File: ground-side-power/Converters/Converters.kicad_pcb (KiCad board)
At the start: 2 copper layers, 82.8 x 74.4 mm, 36 parts, among them J10 Conn_01x03_Female, J12 Conn_01x04_Female, J13 DAQ Voltage Sensing, J14 DAQ Current Sensing, J27 Conn_01x02_Female, U3 K7805-3AR3, U4 INA180, U5 INA180, U6 URB2424LD-20WR3

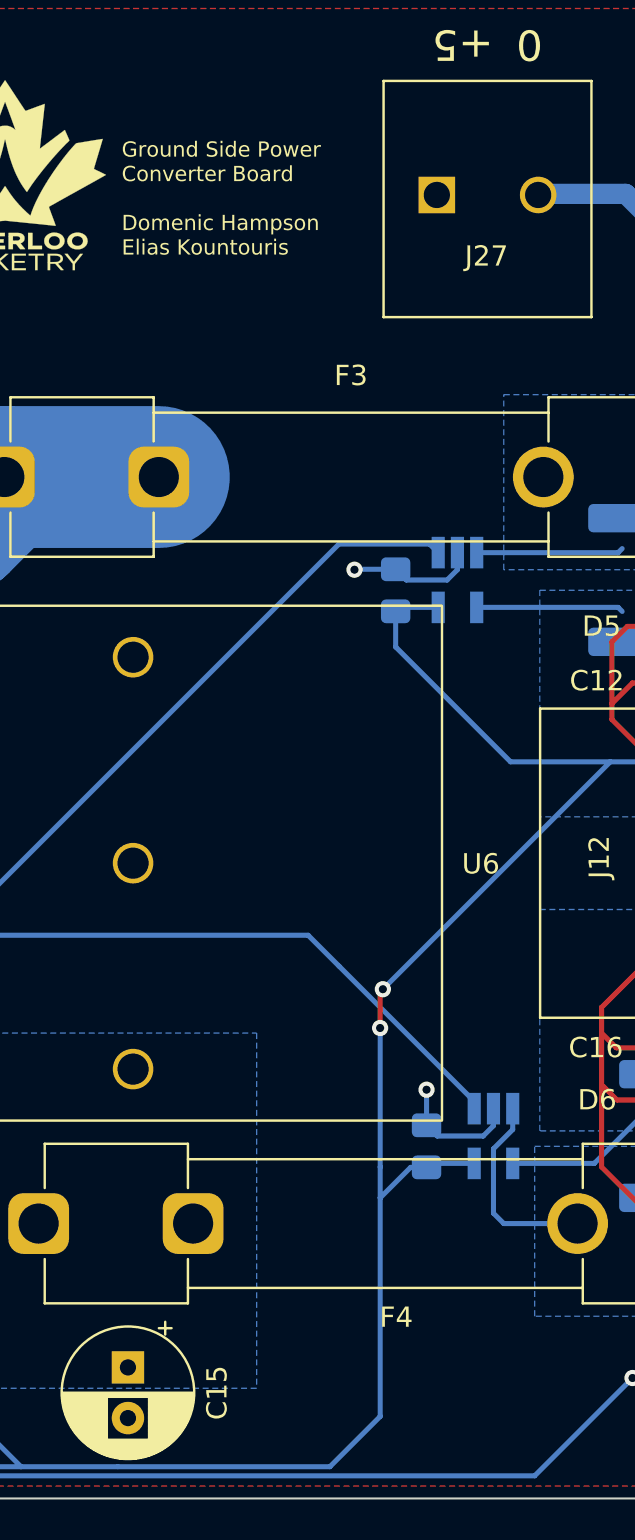
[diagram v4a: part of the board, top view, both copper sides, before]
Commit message: Silkscreen and current sense changes
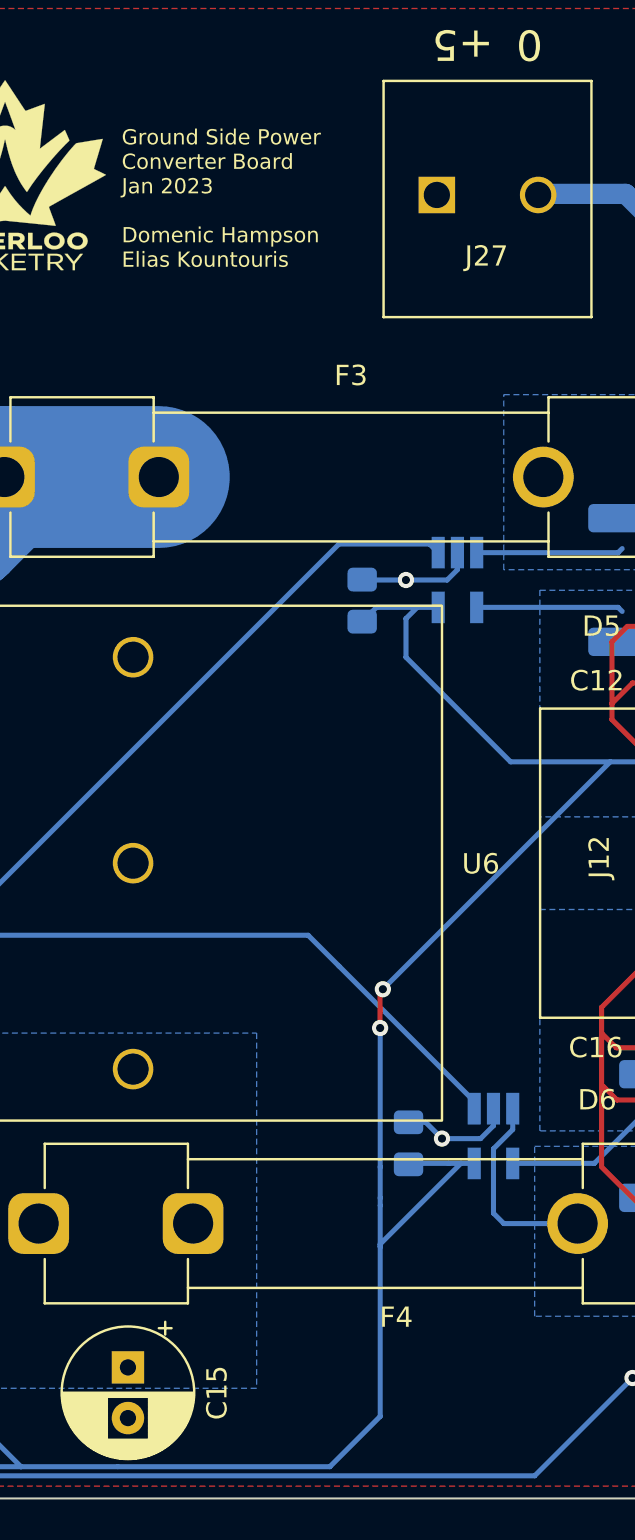
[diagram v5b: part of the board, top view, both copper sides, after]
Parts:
- moved C9 1.73 mm to (161.2, 96.5)
- moved C13 0.90 mm to (163.4, 123.3)
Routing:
- net +5V: track 152.5 -> 158.2 mm
- net GND: track 28.0 -> 26.2 mm
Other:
- board text added: "Ground Side Power Converter Board Jan 2023 Domenic Hampson Elias Kountouris"
- board text removed: "Ground Side Power Converter Board Domenic Hampson Elias Kountouris"
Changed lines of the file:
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@@
   )
   (footprint "Capacitor_SMD:C_0805_2012Metric_Pad1.18x1.45mm_HandSolder" (layer "B.Cu")
-    (at 164.338 123.444 -90)
+    (at 163.449 123.2955 -90)
     (descr "Capacitor SMD 0805 (2012 Metric), square (rectangular) end terminal, IPC_7351 nominal with elongated pad for handsoldering. (Body size source: IPC-SM-782 page 76, https://www.pcb-3d.com/wordpress/wp-content/uploads/ipc-sm-782a_amendment_1_and_2.pdf, https://docs.google.com/spreadsheets/d/1BsfQQcO9C6DZCsRaXUlFlo91Tg2WpOkGARC1WS5S8t0/edit?usp=sharing), generated with kicad-footprint-generator")
     (tags "capacitor handsolder")
@@
   )
   (footprint "Capacitor_SMD:C_0805_2012Metric_Pad1.18x1.45mm_HandSolder" (layer "B.Cu")
-    (at 162.814 96.012 -90)
+    (at 161.163 96.52 -90)
     (descr "Capacitor SMD 0805 (2012 Metric), square (rectangular) end terminal, IPC_7351 nominal with elongated pad for handsoldering. (Body size source: IPC-SM-782 page 76, https://www.pcb-3d.com/wordpress/wp-content/uploads/ipc-sm-782a_amendment_1_and_2.pdf, https://docs.google.com/spreadsheets/d/1BsfQQcO9C6DZCsRaXUlFlo91Tg2WpOkGARC1WS5S8t0/edit?usp=sharing), generated with kicad-footprint-generator")
     (tags "capacitor handsolder")
@@
     (effects (font (size 1.5 1.5) (thickness 0.3)))
   )
-  (gr_text "Ground Side Power\nConverter Board\n\nDomenic Hampson \nElias Kountouris" (at 149.294 76.684) (layer "F.SilkS")
+  (gr_text "Ground Side Power\nConverter Board\nJan 2023\n\nDomenic Hampson \nElias Kountouris" (at 149.294 76.684) (layer "F.SilkS")
     (effects (font (size 0.75 0.75) (thickness 0.15)) (justify left))
   )
@@
     (effects (font (size 1.5 1.5) (thickness 0.3)))
   )
-  (via (at 160.782 94.996) (size 0.8) (drill 0.4) (layers "F.Cu" "B.Cu") (net 1))
+  (via (at 163.322 95.504) (size 0.8) (drill 0.4) (layers "F.Cu" "B.Cu") (net 1))
   (via (at 133.35 135.636) (size 0.8) (drill 0.4) (layers "F.Cu" "B.Cu") (net 1))
-  (via (at 164.338 120.65) (size 0.8) (drill 0.4) (layers "F.Cu" "B.Cu") (net 1))
+  (via (at 165.1 123.063) (size 0.8) (drill 0.4) (layers "F.Cu" "B.Cu") (net 1))
   (via (at 123.19 135.636) (size 0.8) (drill 0.4) (layers "F.Cu" "B.Cu") (net 1))
   (via (at 112.014 138.684) (size 0.8) (drill 0.4) (layers "F.Cu" "B.Cu") (net 1))
-  (segment (start 164.338 122.4065) (end 164.338 120.65) (width 0.25) (layer "B.Cu") (net 1))
   (segment (start 125.1215 91.186) (end 125.1215 88.7465) (width 0.25) (layer "B.Cu") (net 1))
-  (segment (start 163.3435 95.504) (end 165.354 95.504) (width 0.25) (layer "B.Cu") (net 1))
-  (segment (start 162.814 94.9745) (end 160.8035 94.9745) (width 0.25) (layer "B.Cu") (net 1))
+  (segment (start 167.005 123.063) (end 167.64 122.428) (width 0.25) (layer "B.Cu") (net 1))
   (segment (start 114.824 137.16) (end 113.538 137.16) (width 0.25) (layer "B.Cu") (net 1))
-  (segment (start 160.8035 94.9745) (end 160.782 94.996) (width 0.25) (layer "B.Cu") (net 1))
   (segment (start 113.538 137.16) (end 112.014 138.684) (width 0.25) (layer "B.Cu") (net 1))
+  (segment (start 167.64 122.428) (end 167.64 121.586) (width 0.25) (layer "B.Cu") (net 1))
+  (segment (start 165.1 123.063) (end 167.005 123.063) (width 0.25) (layer "B.Cu") (net 1))
   (segment (start 125.289 88.579) (end 125.289 87.63) (width 0.25) (layer "B.Cu") (net 1))
   (segment (start 120.209 90.7115) (end 120.209 87.63) (width 0.25) (layer "B.Cu") (net 1))
-  (segment (start 164.8675 122.936) (end 167.132 122.936) (width 0.25) (layer "B.Cu") (net 1))
   (segment (start 165.354 95.504) (end 165.862 94.996) (width 0.25) (layer "B.Cu") (net 1))
   (segment (start 124.714 137.16) (end 123.19 135.636) (width 0.25) (layer "B.Cu") (net 1))
-  (segment (start 162.814 94.9745) (end 163.3435 95.504) (width 0.25) (layer "B.Cu") (net 1))
-  (segment (start 167.64 122.428) (end 167.64 121.586) (width 0.25) (layer "B.Cu") (net 1))
+  (segment (start 164.295 122.258) (end 165.1 123.063) (width 0.25) (layer "B.Cu") (net 1))
   (segment (start 134.636 137.16) (end 134.636 136.922) (width 0.25) (layer "B.Cu") (net 1))
+  (segment (start 163.449 122.258) (end 164.295 122.258) (width 0.25) (layer "B.Cu") (net 1))
   (segment (start 119.7345 91.186) (end 120.209 90.7115) (width 0.25) (layer "B.Cu") (net 1))
+  (segment (start 163.322 95.504) (end 161.6925 95.504) (width 0.25) (layer "B.Cu") (net 1))
   (segment (start 125.1215 88.7465) (end 125.289 88.579) (width 0.25) (layer "B.Cu") (net 1))
-  (segment (start 164.338 122.4065) (end 164.8675 122.936) (width 0.25) (layer "B.Cu") (net 1))
-  (segment (start 167.132 122.936) (end 167.64 122.428) (width 0.25) (layer "B.Cu") (net 1))
   (segment (start 124.984 137.16) (end 124.714 137.16) (width 0.25) (layer "B.Cu") (net 1))
   (segment (start 165.862 94.996) (end 165.862 94.154) (width 0.25) (layer "B.Cu") (net 1))
   (segment (start 134.636 136.922) (end 133.35 135.636) (width 0.25) (layer "B.Cu") (net 1))
+  (segment (start 165.354 95.504) (end 163.322 95.504) (width 0.25) (layer "B.Cu") (net 1))
   (segment (start 174.498 100.584) (end 173.482 101.6) (width 0.25) (layer "F.Cu") (net 2))
   (segment (start 173.482 98.552) (end 174.244 97.79) (width 0.25) (layer "F.Cu") (net 2))
@@
   (via (at 162.047701 117.606299) (size 0.8) (drill 0.4) (layers "F.Cu" "B.Cu") (net 2))
   (via (at 162.183299 115.692701) (size 0.8) (drill 0.4) (layers "F.Cu" "B.Cu") (net 2))
-  (segment (start 162.814 98.806) (end 168.482001 104.474001) (width 0.25) (layer "B.Cu") (net 2))
+  (segment (start 163.322 97.409) (end 163.322 99.314) (width 0.25) (layer "B.Cu") (net 2))
+  (segment (start 163.877 96.854) (end 161.8665 96.854) (width 0.25) (layer "B.Cu") (net 2))
+  (segment (start 161.8665 96.854) (end 161.163 97.5575) (width 0.25) (layer "B.Cu") (net 2))
   (segment (start 159.57 139.25) (end 162.052 136.768) (width 0.25) (layer "B.Cu") (net 2))
-  (segment (start 163.0095 96.854) (end 162.814 97.0495) (width 0.25) (layer "B.Cu") (net 2))
-  (segment (start 164.5335 124.286) (end 164.338 124.4815) (width 0.25) (layer "B.Cu") (net 2))
-  (segment (start 164.912 96.854) (end 163.0095 96.854) (width 0.25) (layer "B.Cu") (net 2))
+  (segment (start 168.482001 104.474001) (end 173.401999 104.474001) (width 0.25) (layer "B.Cu") (net 2))
   (segment (start 162.052 125.984) (end 162.052 124.46) (width 0.25) (layer "B.Cu") (net 2))
   (segment (start 162.183299 115.692701) (end 173.401999 104.474001) (width 0.25) (layer "B.Cu") (net 2))
@@
   (segment (start 142.52 137.44) (end 144.33 139.25) (width 0.25) (layer "B.Cu") (net 2))
   (segment (start 142.52 137.16) (end 142.52 137.44) (width 0.25) (layer "B.Cu") (net 2))
-  (segment (start 168.482001 104.474001) (end 173.401999 104.474001) (width 0.25) (layer "B.Cu") (net 2))
+  (segment (start 163.322 99.314) (end 168.482001 104.474001) (width 0.25) (layer "B.Cu") (net 2))
   (segment (start 133.662 139.25) (end 144.33 139.25) (width 0.25) (layer "B.Cu") (net 2))
   (segment (start 162.052 124.46) (end 162.052 117.610598) (width 0.25) (layer "B.Cu") (net 2))
-  (segment (start 164.338 124.4815) (end 163.5545 124.4815) (width 0.25) (layer "B.Cu") (net 2))
+  (segment (start 166.69 124.286) (end 166.036 124.286) (width 0.25) (layer "B.Cu") (net 2))
+  (segment (start 165.434 124.286) (end 163.623 124.286) (width 0.25) (layer "B.Cu") (net 2))
   (segment (start 173.79 96.854) (end 166.812 96.854) (width 0.25) (layer "B.Cu") (net 2))
   (segment (start 175.567999 104.474001) (end 181.102 98.94) (width 1) (layer "B.Cu") (net 2))
+  (segment (start 162.052 136.768) (end 162.052 128.397) (width 0.25) (layer "B.Cu") (net 2))
+  (segment (start 164.912 96.854) (end 163.877 96.854) (width 0.25) (layer "B.Cu") (net 2))
   (segment (start 173.99 97.054) (end 173.79 96.854) (width 0.25) (layer "B.Cu") (net 2))
+  (segment (start 162.052 126.365) (end 162.052 125.984) (width 0.25) (layer "B.Cu") (net 2))
   (segment (start 131.572 137.16) (end 133.662 139.25) (width 0.25) (layer "B.Cu") (net 2))
+  (segment (start 162.052 128.397) (end 162.052 126.365) (width 0.25) (layer "B.Cu") (net 2))
   (segment (start 162.052 117.610598) (end 162.047701 117.606299) (width 0.25) (layer "B.Cu") (net 2))
-  (segment (start 162.052 136.768) (end 162.052 125.984) (width 0.25) (layer "B.Cu") (net 2))
-  (segment (start 162.814 97.0495) (end 162.814 98.806) (width 0.25) (layer "B.Cu") (net 2))
-  (segment (start 163.5545 124.4815) (end 162.052 125.984) (width 0.25) (layer "B.Cu") (net 2))
-  (segment (start 166.69 124.286) (end 164.5335 124.286) (width 0.25) (layer "B.Cu") (net 2))
+  (segment (start 166.036 124.286) (end 165.434 124.286) (width 0.25) (layer "B.Cu") (net 2))
+  (segment (start 163.877 96.854) (end 163.322 97.409) (width 0.25) (layer "B.Cu") (net 2))
   (segment (start 173.401999 104.474001) (end 175.567999 104.474001) (width 0.25) (layer "B.Cu") (net 2))
   (segment (start 149.098 139.25) (end 159.57 139.25) (width 0.25) (layer "B.Cu") (net 2))
+  (segment (start 162.052 128.27) (end 162.052 128.397) (width 0.25) (layer "B.Cu") (net 2))
+  (segment (start 166.036 124.286) (end 162.052 128.27) (width 0.25) (layer "B.Cu") (net 2))
   (segment (start 181.102 98.94) (end 181.102 83.392) (width 1) (layer "B.Cu") (net 2))
   (segment (start 181.102 83.392) (end 174.164 76.454) (width 1) (layer "B.Cu") (net 2))
+  (segment (start 163.623 124.286) (end 163.576 124.333) (width 0.25) (layer "B.Cu") (net 2))
   (segment (start 132.468 91.186) (end 132.909 90.745) (width 0.25) (layer "B.Cu") (net 3))
   (segment (start 143.51 90.424) (end 151.13 90.424) (width 7) (layer "B.Cu") (net 3))

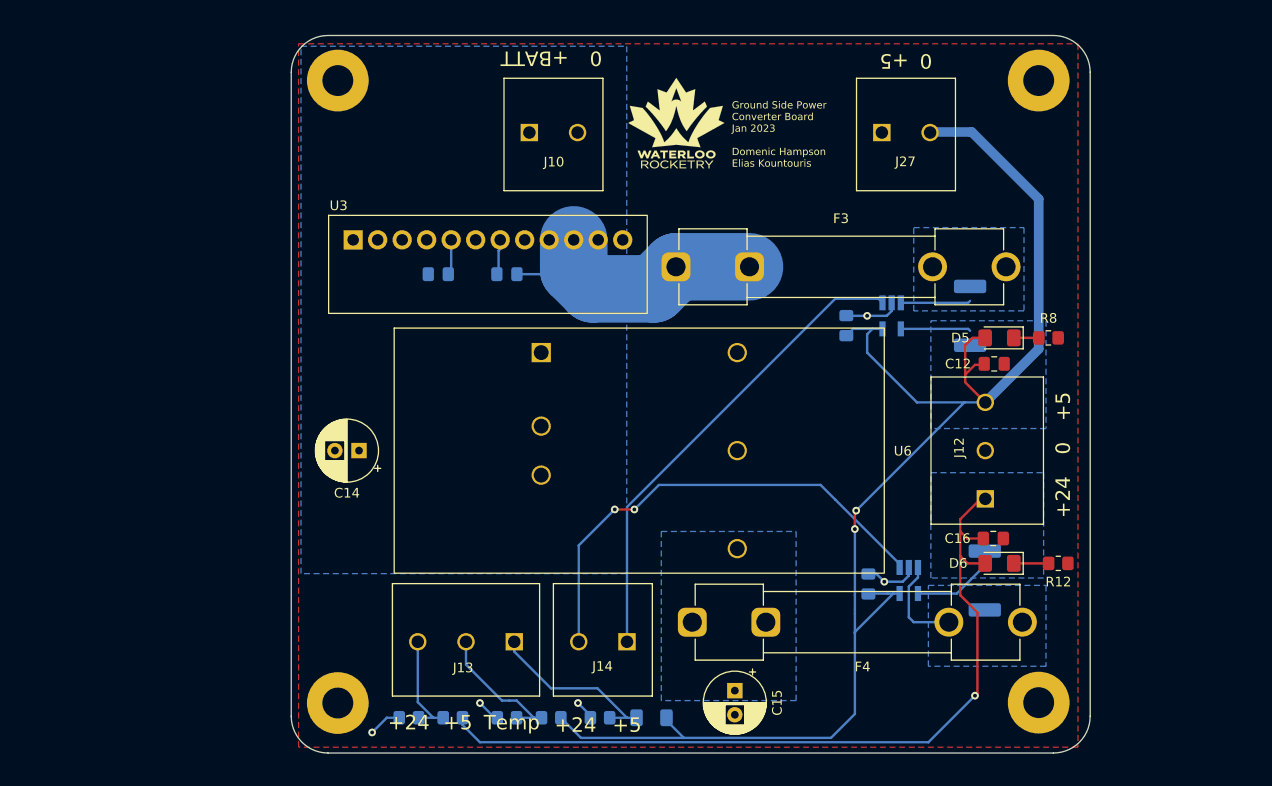
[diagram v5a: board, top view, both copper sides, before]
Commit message: Updated Fuses
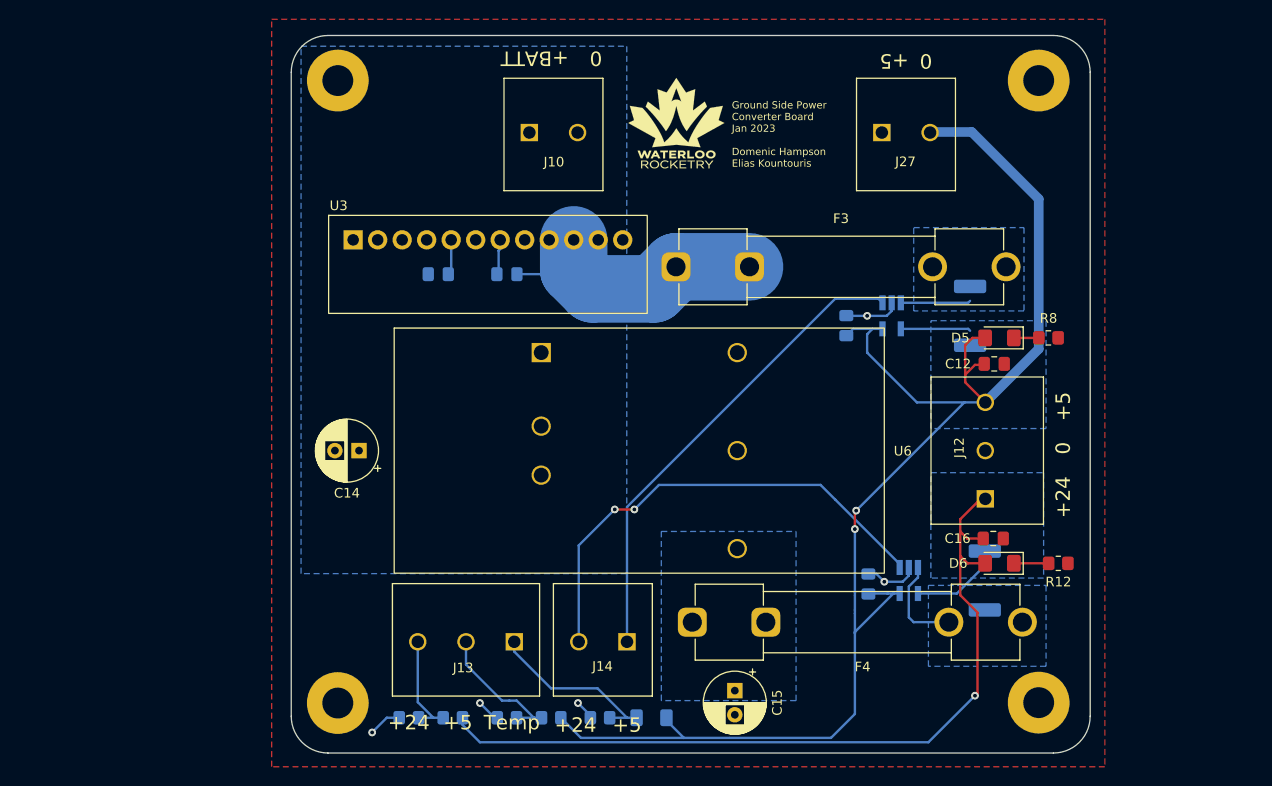
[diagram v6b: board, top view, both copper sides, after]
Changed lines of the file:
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@@
     (connect_pads yes (clearance 0.508))
     (min_thickness 0.254) (filled_areas_thickness no)
-    (fill yes (thermal_gap 0.508) (thermal_bridge_width 0.508))
+    (fill (thermal_gap 0.508) (thermal_bridge_width 0.508))
     (polygon
       (pts
-        (xy 185.166 140.208)
-        (xy 104.394 140.208)
-        (xy 104.394 67.31)
-        (xy 185.166 67.31)
+        (xy 187.96 142.24)
+        (xy 101.6 142.24)
+        (xy 101.6 64.77)
+        (xy 187.96 64.77)
       )
     )
